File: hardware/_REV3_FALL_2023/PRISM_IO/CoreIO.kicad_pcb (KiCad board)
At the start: 2 copper layers, 61 x 88.9 mm, 40 parts, among them J1 Conn_01x04_Socket, J2 COTS_SWITCH_PLUG, J3 PYRO 1, J4 PYRO 2, J5 Conn_01x04_Socket, Q1 AO3400A, Q2 AO3400A, U1 TMC2209_SILENTSTEPSTICK, U2 LD1117S12TR_SOT223

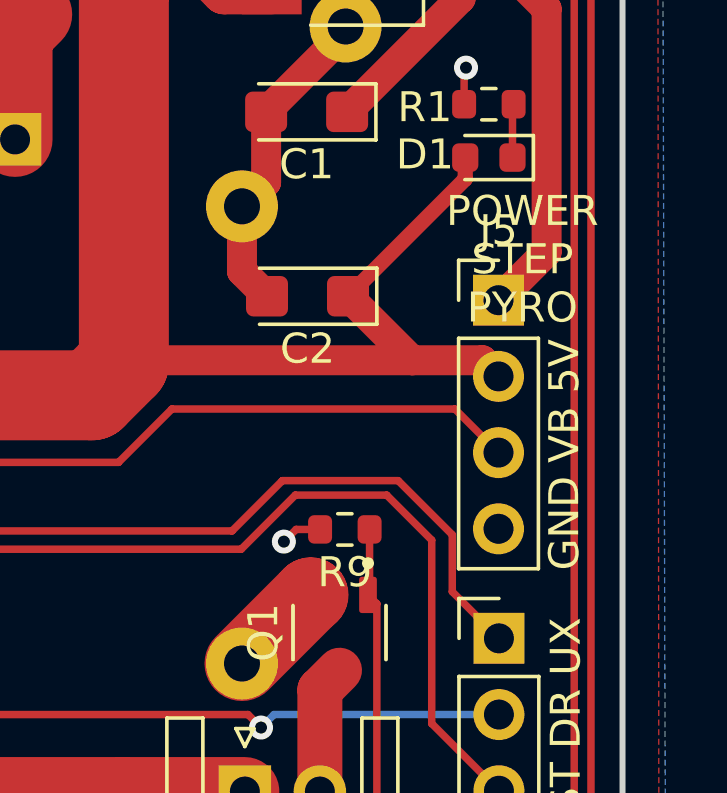
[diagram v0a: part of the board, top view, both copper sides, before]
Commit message: Fix silk on IO
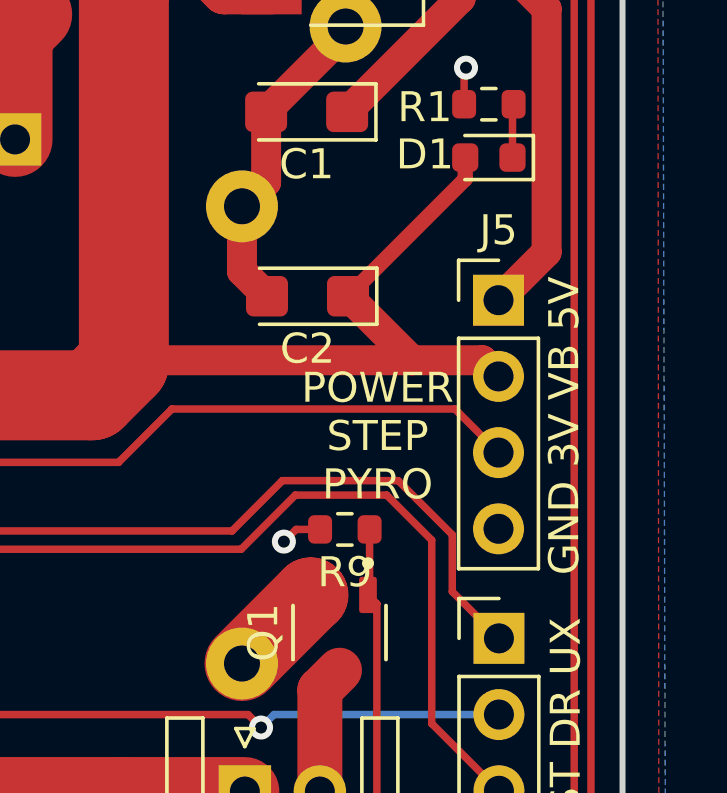
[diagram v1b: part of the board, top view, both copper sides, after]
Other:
- board text added: "GND 3V VB 5V"
- board text removed: "GND VB 5V"

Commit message: Production Main Avionics Boards
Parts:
- moved U2 2.09 mm to (170.3, 86.4)
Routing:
- net /5V: track 28.6 -> 31.2 mm
- net GND: track 27.6 -> 25.6 mm, vias 7 -> 9
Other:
- board text added: "Jojo Liu"
- board text added: "Rishit Bansal"
- board text removed: "Joseph Liu"
